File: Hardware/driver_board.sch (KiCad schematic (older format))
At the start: 48 parts, among them P1 CONN_4X2, P10 CONN_4X2, P11 CONN_4X2, P12 CONN_4X2, P13 CONN_4X2, P14 CONN_4X2, P15 CONN_4X2, P16 CONN_4X2, P17 CONN_4X2, P18 CONN_4X2, P19 CONN_4X2, P2 CONN_4X2, P20 CONN_4X2, P21 CONN_4X2, P22 CONN_4X2, P23 CONN_4X2, P24 CONN_4X2, P3 CONN_4X2, P4 CONN_4X2, P5 CONN_4X2, P6 CONN_4X2, P7 CONN_4X2, P8 CONN_4X2, P9 CONN_4X2, U1 TLC590, U10 TLC590, U11 TLC590, U12 TLC590, U2 TLC590, U3 TLC590, U4 TLC590, U5 TLC590, U6 TLC590, U7 TLC590, U8 TLC590, U9 TLC590

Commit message: progress on board
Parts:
- added C1, C10, C11, C12, C2, C3, C4, C5, C6, C7, C8, C9: C, Capacitors_SMD:c_0805, symbol C
- added P25, P26, P27: CONN_4X2, Pin_Headers:Pin_Header_Straight_2x04, symbol CONN_4X2
- added R13: R, Resistors_SMD:Resistor_SMD0805_HandSoldering, symbol R
- P1, P10, P11, P12, P13, P14, P15, P16, P17, P18, P19, P2, P20, P21, P22, P23, P24, P3, P4, P5, P6, P7, P8, P9: footprint (none) -> Pin_Headers:Pin_Header_Straight_2x04
- R1, R10, R11, R12, R2, R3, R4, R5, R6, R7, R8, R9: footprint (none) -> Resistors_SMD:Resistor_SMD0805_HandSoldering
- U1, U10, U11, U12, U2, U3, U4, U5, U6, U7, U8, U9: footprint (none) -> TLC5940:SSOP-28H
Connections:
- net labels added: +3.3V, L1, L2, L3, L4, L5, L6, L7, L8
- wire segments 30 -> 92
- no-connect marks 0 -> 3

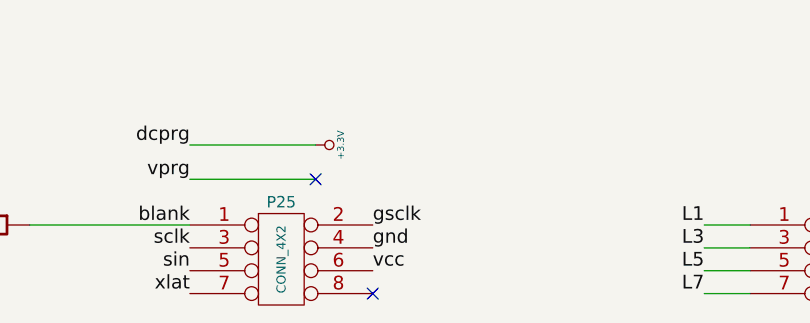
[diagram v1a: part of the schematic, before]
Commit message: moving from kicad to eagle. The boards came ba ck with crazy shorts in them so i am re-designing them in kicad.
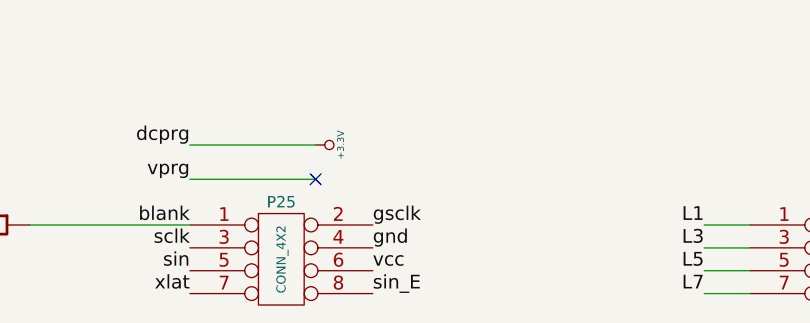
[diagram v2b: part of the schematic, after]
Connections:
- no-connect marks 3 -> 2
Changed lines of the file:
@@
 $EndComp
 $Comp
-L GND #PWR028
+L GND #PWR027
 U 1 1 53ABF2A1
 P 7950 3950
-F 0 "#PWR028" H 7950 3950 30  0001 C CNN
+F 0 "#PWR027" H 7950 3950 30  0001 C CNN
 F 1 "GND" H 7950 3880 30  0001 C CNN
 F 2 "" H 7950 3950 60  0000 C CNN
@@
 	1    0    0    -1
 $EndComp
-NoConn ~ 5200 13000
 NoConn ~ 21800 4150
 NoConn ~ 4950 12500
+Text Label 5200 13000 0    60   ~ 0
+sin_E
 $EndSCHEMATC
